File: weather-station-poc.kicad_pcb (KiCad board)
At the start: 2 copper layers, 131 parts, among them IC1 632723100011, IC2 TCPP01-M12, IC3 USBLC6-2SC6, IC4 BME690, IC5 S2-LPQTR, IC6 BALF-SPI2-01D3, IC7 STSAFA110S8OCD03, J1 Conn_ARM_JTAG_SWD_10, J2 61300311121, J3 61300311121, J4 61300511121, J5 61300311121, J6 687140149022, J7 687110149022, Q1 STL11N3LLH6, U1 STM32U5G9ZJTxQ, U2 BME280, U3 BMP581, Y1 NX2016SA-16MHZ-EXS00A-CS07826, Y2 NX2012SA-32.768K-STD-MUB-1, Y3 NX1612SA-50M-EXS00A-CS08403

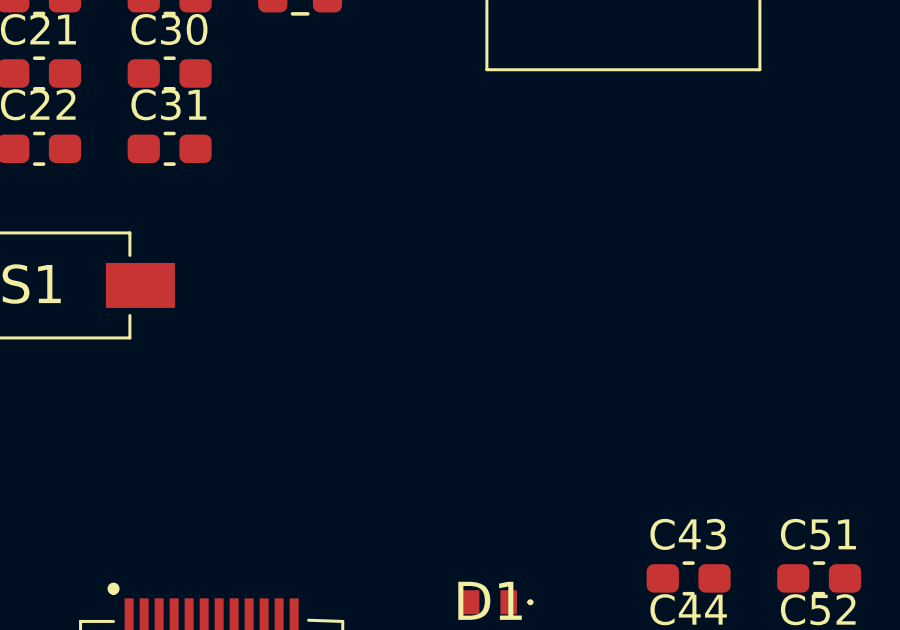
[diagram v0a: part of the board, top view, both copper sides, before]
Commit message: Add a new reference for L6 inductor on boost converter
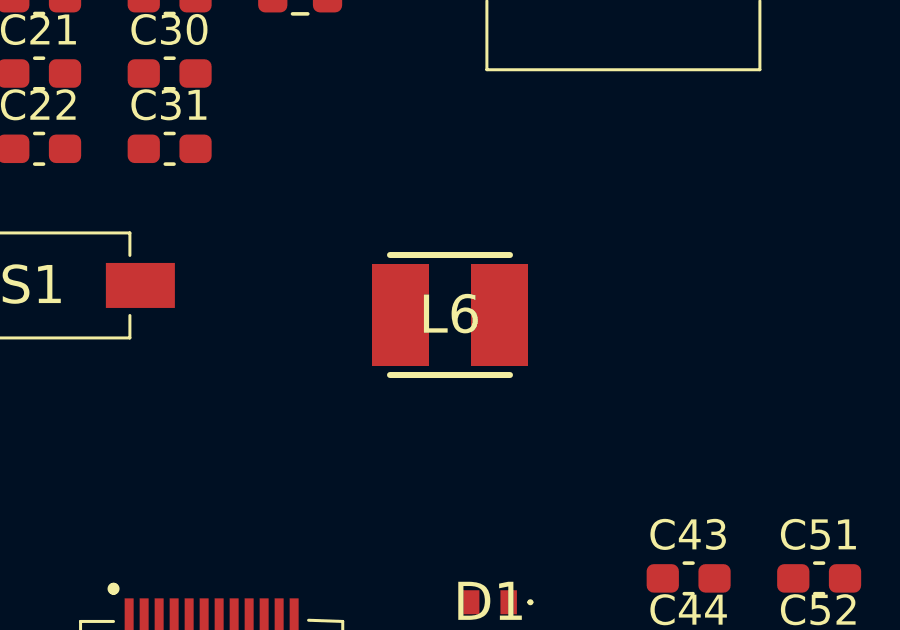
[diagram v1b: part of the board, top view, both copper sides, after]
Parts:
- added L6: 10u, weather-station-poc-fp:INDPM4040X180N, F.Cu at (165.5, 82.0)
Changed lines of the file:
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@@
+		)
+	)
+	(footprint "weather-station-poc-fp:INDPM4040X180N"
+		(layer "F.Cu")
+		(at 165.525 82)
+		(descr "4018")
+		(tags "Inductor")
+		(property "Reference" "L6"
+			(at 0 0 0)
+			(layer "F.SilkS")
+			(effects
+				(font
+					(size 1.27 1.27)
+					(thickness 0.254)
+				)
+			)
+		)
+		(property "Value" "10u"
+			(at 0 0 0)
+			(layer "F.SilkS")
+			(hide yes)
+			(effects
+				(font
+					(size 1.27 1.27)
+					(thickness 0.254)
+				)
+			)
+		)
+		(property "Datasheet" "https://www.we-online.com/components/products/datasheet/74404042100.pdf"
+			(at 0 0 0)
+			(layer "F.Fab")
+			(hide yes)
+			(effects
+				(font
+					(size 1.27 1.27)
+					(thickness 0.15)
+				)
+			)
+		)
+		(property "Description" "Inductor"
+			(at 0 0 0)
+			(layer "F.Fab")
+			(hide yes)
+			(effects
+				(font
+					(size 1.27 1.27)
+					(thickness 0.15)
+				)
+			)
+		)
+		(property ki_fp_filters "Choke_* *Coil* Inductor_* L_*")
+		(sheetname "/Power/")
+		(sheetfile "power.kicad_sch")
+		(attr smd)
+		(fp_line
+			(start -2 2)
+			(end 2 2)
+			(stroke
+				(width 0.2)
+				(type solid)
+			)
+			(layer "F.SilkS")
+		)
+		(fp_line
+			(start 2 -2)
+			(end -2 -2)
+			(stroke
+				(width 0.2)
+				(type solid)
+			)
+			(layer "F.SilkS")
+		)
+		(fp_line
+			(start -2.85 -2.35)
+			(end 2.85 -2.35)
+			(stroke
+				(width 0.05)
+				(type solid)
+			)
+			(layer "F.CrtYd")
+		)
+		(fp_line
+			(start -2.85 2.35)
+			(end -2.85 -2.35)
+			(stroke
+				(width 0.05)
+				(type solid)
+			)
+			(layer "F.CrtYd")
+		)
+		(fp_line
+			(start 2.85 -2.35)
+			(end 2.85 2.35)
+			(stroke
+				(width 0.05)
+				(type solid)
+			)
+			(layer "F.CrtYd")
+		)
+		(fp_line
+			(start 2.85 2.35)
+			(end -2.85 2.35)
+			(stroke
+				(width 0.05)
+				(type solid)
+			)
+			(layer "F.CrtYd")
+		)
+		(fp_line
+			(start -2 -2)
+			(end 2 -2)
+			(stroke
+				(width 0.1)
+				(type solid)
+			)
+			(layer "F.Fab")
+		)
+		(fp_line
+			(start -2 2)
+			(end -2 -2)
+			(stroke
+				(width 0.1)
+				(type solid)
+			)
+			(layer "F.Fab")
+		)
+		(fp_line
+			(start 2 -2)
+			(end 2 2)
+			(stroke
+				(width 0.1)
+				(type solid)
+			)
+			(layer "F.Fab")
+		)
+		(fp_line
+			(start 2 2)
+			(end -2 2)
+			(stroke
+				(width 0.1)
+				(type solid)
+			)
+			(layer "F.Fab")
+		)
+		(fp_text user "${REFERENCE}"
+			(at 0 0 0)
+			(layer "F.Fab")
+			(effects
+				(font
+					(size 1.27 1.27)
+					(thickness 0.254)
+				)
+			)
+		)
+		(pad "1" smd rect
+			(at -1.65 0)
+			(size 1.9 3.4)
+			(layers "F.Cu" "F.Mask" "F.Paste")
+			(net 27 "Net-(PS2-VIN)")
+			(pinfunction "1")
+			(pintype "passive")
+		)
+		(pad "2" smd rect
+			(at 1.65 0)
+			(size 1.9 3.4)
+			(layers "F.Cu" "F.Mask" "F.Paste")
+			(net 28 "Net-(D3-A)")
+			(pinfunction "2")
+			(pintype "passive")
+		)
+		(embedded_fonts no)
+		(model "74404042100.stp"
+			(offset
+				(xyz 0 0 0)
+			)
+			(scale
+				(xyz 1 1 1)
+			)
+			(rotate
+				(xyz 0 0 0)
+			)
 		)
 	)

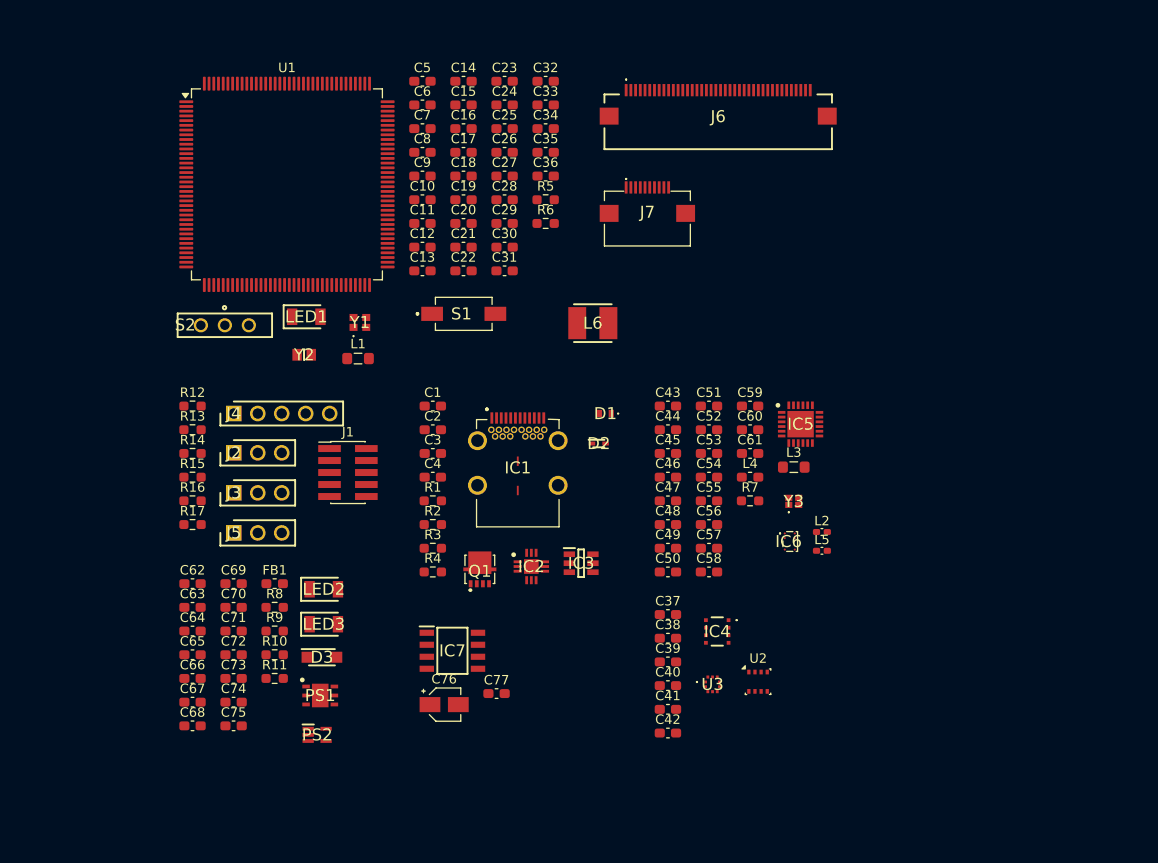
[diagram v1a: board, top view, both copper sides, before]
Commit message: Update PCB layout and remove unused PDF
Deleted the unused DS_RVT50HQTFWCA0_Rev.1.0 (1).pdf from docs. Updated weather-station-poc.kicad_pcb with significant component repositioning, including capacitors, resistors, ICs, LEDs, connectors, and removal of the L6 inductor footprint, reflecting a major board layout revision.
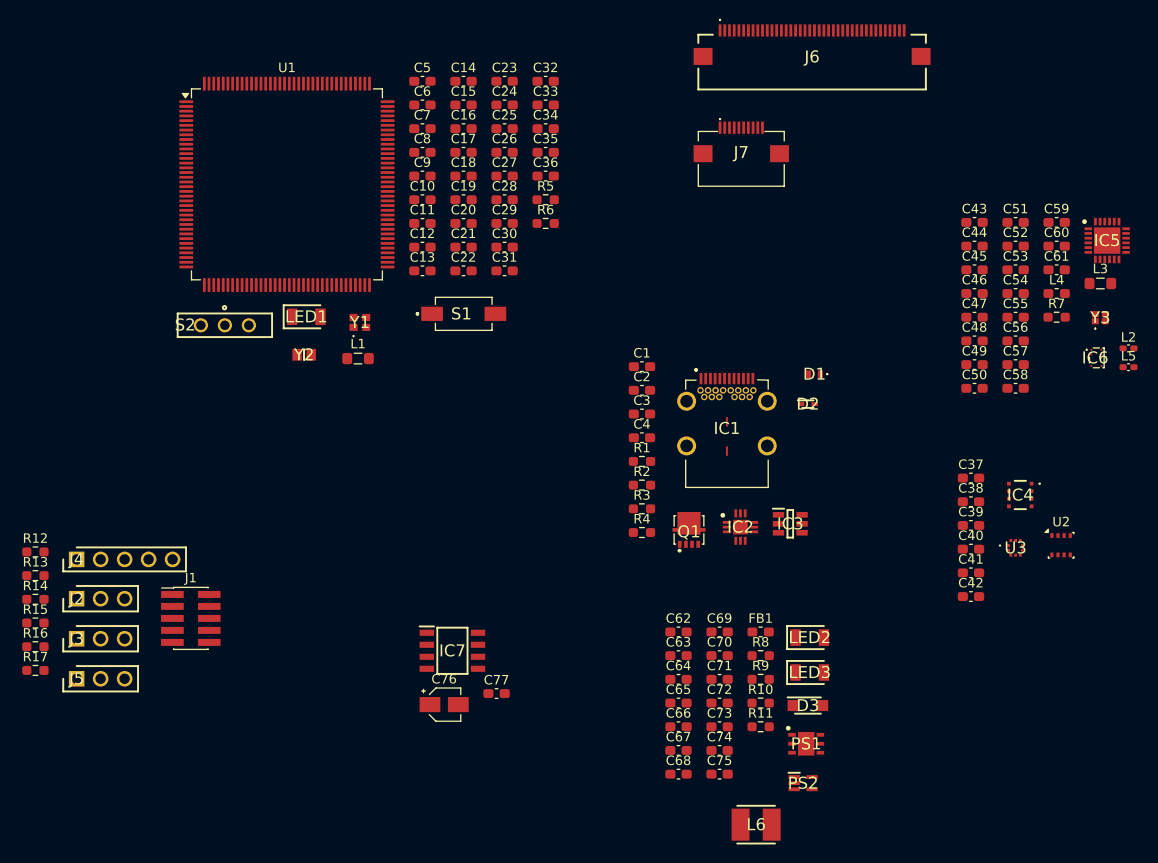
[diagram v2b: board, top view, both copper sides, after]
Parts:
- moved L6 55.9 mm to (182.8, 135.1)
- moved C62 51.7 mm to (174.6, 114.7)
- moved C63 51.7 mm to (174.6, 117.2)
- moved C64 51.7 mm to (174.6, 119.7)
- moved C65 51.7 mm to (174.6, 122.2)
- moved C66 51.7 mm to (174.6, 124.7)
- moved C67 51.7 mm to (174.6, 127.3)
- moved C68 51.7 mm to (174.6, 129.8)
- moved D3 51.7 mm to (188.3, 122.5)
- moved FB1 51.7 mm to (183.3, 114.7)
- moved LED2 51.7 mm to (188.5, 115.3)
- moved LED3 51.7 mm to (188.5, 119.0)
- moved PS1 51.7 mm to (188.1, 126.5)
- moved PS2 51.7 mm to (187.8, 130.7)
- moved R10 51.7 mm to (183.3, 122.2)
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
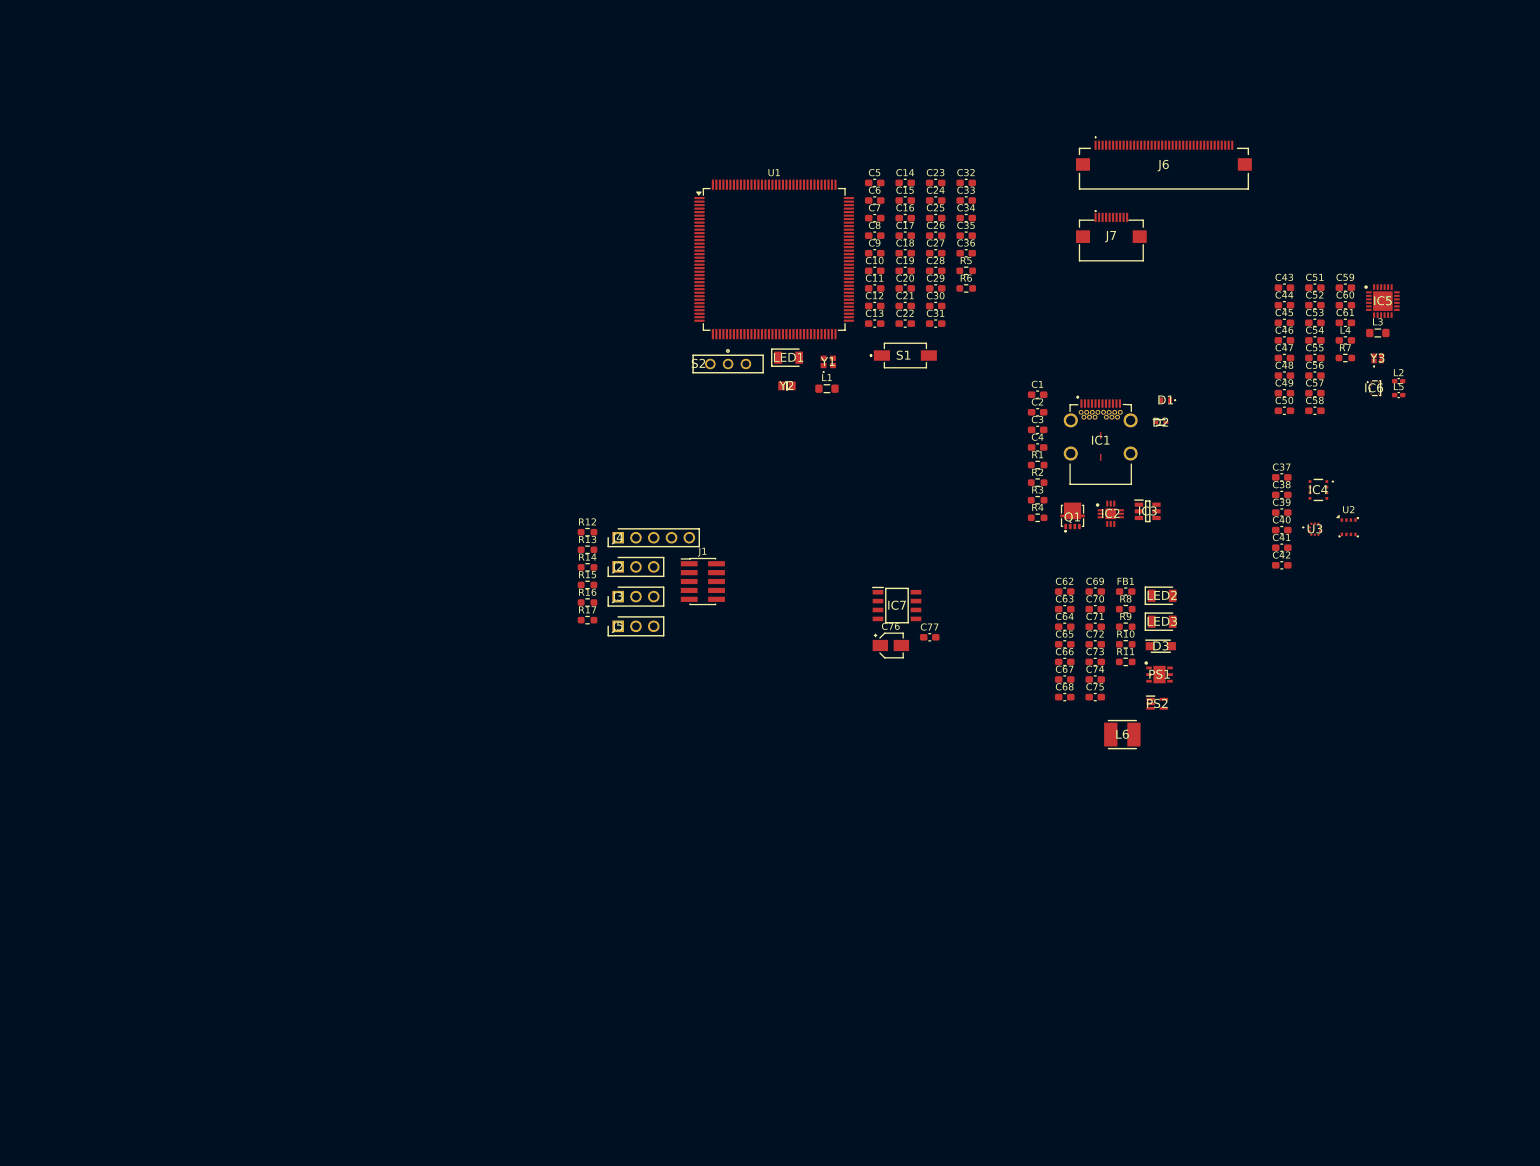
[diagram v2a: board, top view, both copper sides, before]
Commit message: Prepare PCB size with mounting holes
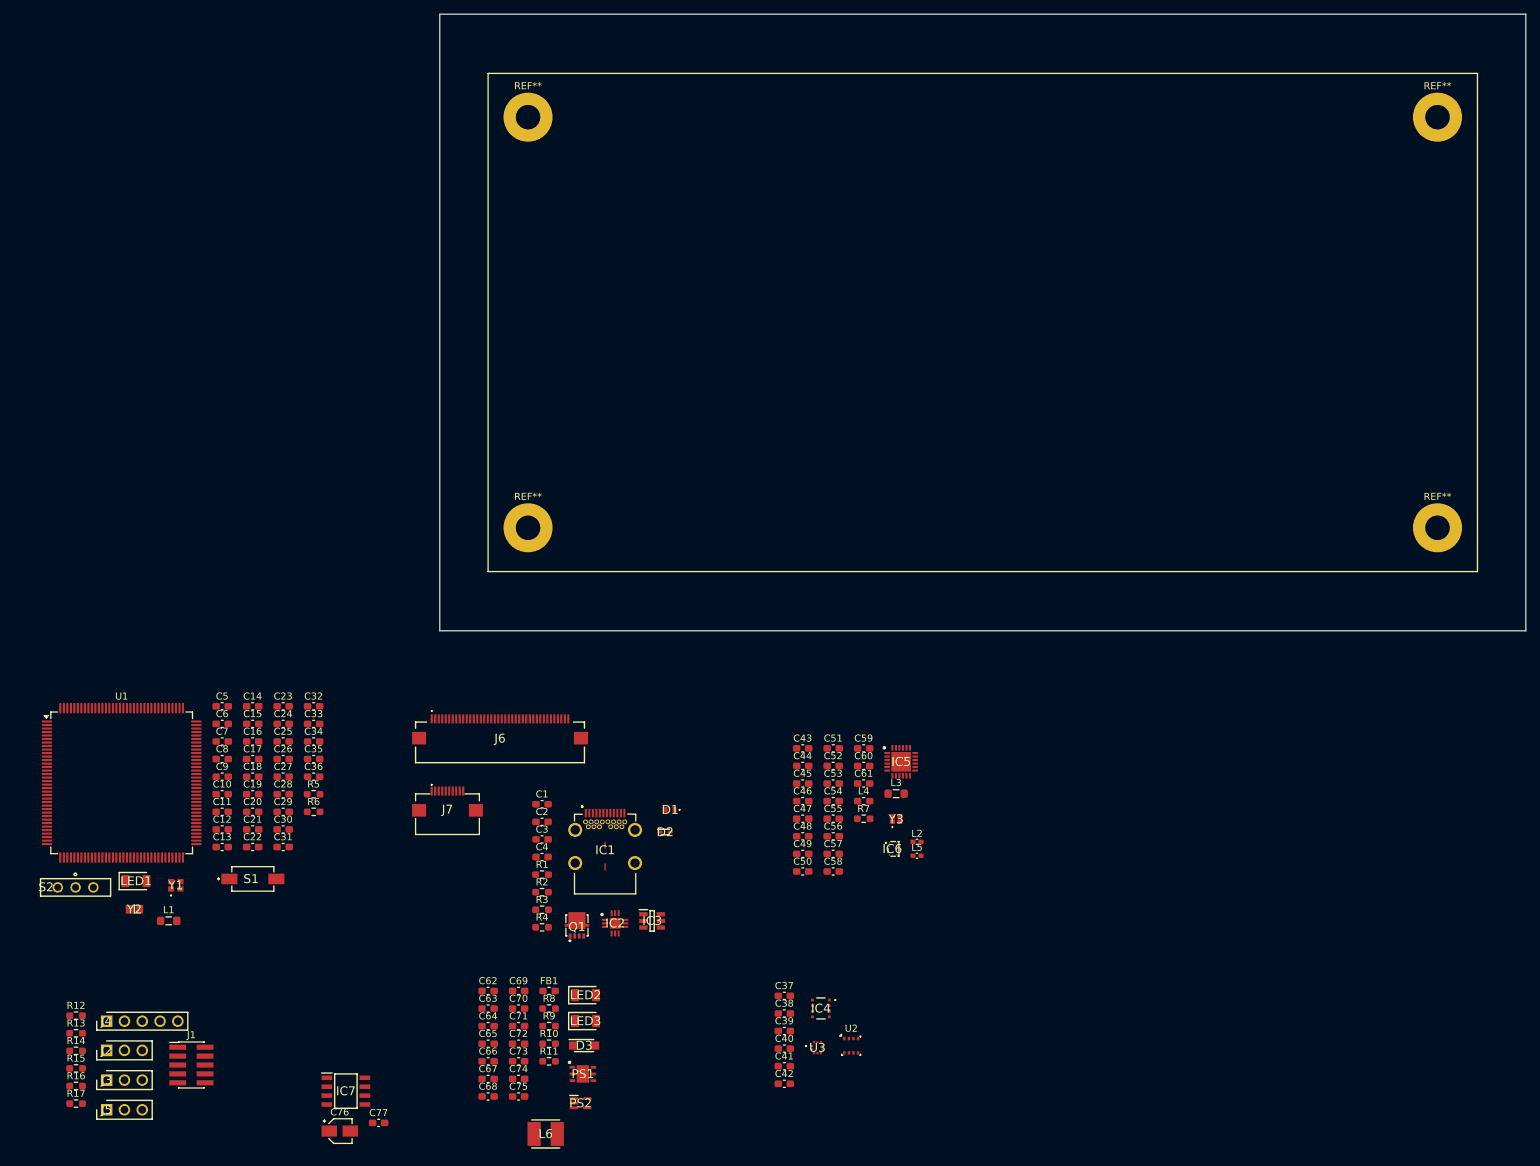
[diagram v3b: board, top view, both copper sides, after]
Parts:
- added REF**: MountingHole_3.5mm_Pad, MountingHole:MountingHole_3.5mm_Pad, F.Cu at (98.0, 105.6)
- added REF**: MountingHole_3.5mm_Pad, MountingHole:MountingHole_3.5mm_Pad, F.Cu at (227.8, 105.6)
- added REF**: MountingHole_3.5mm_Pad, MountingHole:MountingHole_3.5mm_Pad, F.Cu at (227.8, 47.0)
- added REF**: MountingHole_3.5mm_Pad, MountingHole:MountingHole_3.5mm_Pad, F.Cu at (98.0, 47.0)
- moved J6 125.2 mm to (94.0, 136.0)
- moved J7 125.2 mm to (86.5, 143.6)
- moved L1 120.8 mm to (46.7, 161.7)
- moved C32 119.4 mm to (67.4, 131.1)
- moved C35 119.4 mm to (67.4, 138.6)
- moved C5 119.4 mm to (54.4, 131.1)
- moved C8 119.4 mm to (54.4, 138.6)
- moved C14 119.4 mm to (58.7, 131.1)
- moved C15 119.4 mm to (58.7, 133.6)
- moved C16 119.4 mm to (58.7, 136.1)
- moved C17 119.4 mm to (58.7, 138.6)
- moved C18 119.4 mm to (58.7, 141.1)
- moved C19 119.4 mm to (58.7, 143.6)
- moved C20 119.4 mm to (58.7, 146.1)
- moved C21 119.4 mm to (58.7, 148.7)
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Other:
- board outline added: 155 x 88 mm

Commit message: Use 4 layers board
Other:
- copper layers 2 -> 4
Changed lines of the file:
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@@
 	(layers
 		(0 "F.Cu" signal)
+		(4 "In1.Cu" signal)
+		(6 "In2.Cu" signal)
 		(2 "B.Cu" signal)
 		(9 "F.Adhes" user "F.Adhesive")
@@
 	)
 	(setup
+		(stackup
+			(layer "F.SilkS"
+				(type "Top Silk Screen")
+			)
+			(layer "F.Paste"
+				(type "Top Solder Paste")
+			)
+			(layer "F.Mask"
+				(type "Top Solder Mask")
+				(thickness 0.01)
+			)
+			(layer "F.Cu"
+				(type "copper")
+				(thickness 0.035)
+			)
+			(layer "dielectric 1"
+				(type "prepreg")
+				(thickness 0.1)
+				(material "FR4")
+				(epsilon_r 4.5)
+				(loss_tangent 0.02)
+			)
+			(layer "In1.Cu"
+				(type "copper")
+				(thickness 0.035)
+			)
+			(layer "dielectric 2"
+				(type "core")
+				(thickness 1.24)
+				(material "FR4")
+				(epsilon_r 4.5)
+				(loss_tangent 0.02)
+			)
+			(layer "In2.Cu"
+				(type "copper")
+				(thickness 0.035)
+			)
+			(layer "dielectric 3"
+				(type "prepreg")
+				(thickness 0.1)
+				(material "FR4")
+				(epsilon_r 4.5)
+				(loss_tangent 0.02)
+			)
+			(layer "B.Cu"
+				(type "copper")
+				(thickness 0.035)
+			)
+			(layer "B.Mask"
+				(type "Bottom Solder Mask")
+				(thickness 0.01)
+			)
+			(layer "B.Paste"
+				(type "Bottom Solder Paste")
+			)
+			(layer "B.SilkS"
+				(type "Bottom Silk Screen")
+			)
+			(copper_finish "None")
+			(dielectric_constraints no)
+		)
 		(pad_to_mask_clearance 0)
 		(allow_soldermask_bridges_in_footprints no)
